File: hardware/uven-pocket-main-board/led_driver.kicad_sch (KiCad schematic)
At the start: 13 parts, among them U12 SIDR392DP-T1-GE3, U13 SIDR392DP-T1-GE3, U4 TPS2HB50BQPWPRQ1

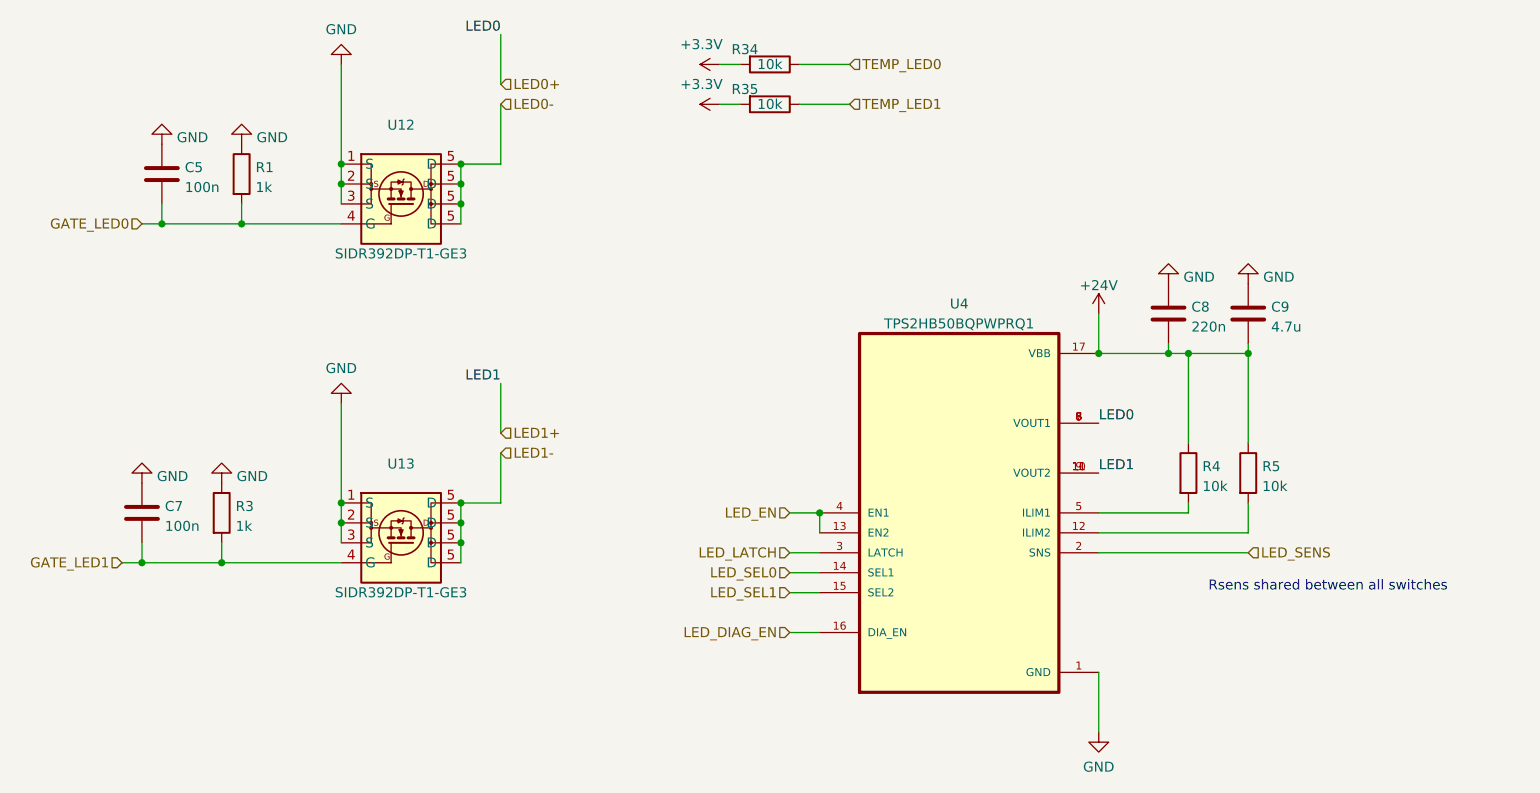
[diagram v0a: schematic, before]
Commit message: uven pocket layout almost finished
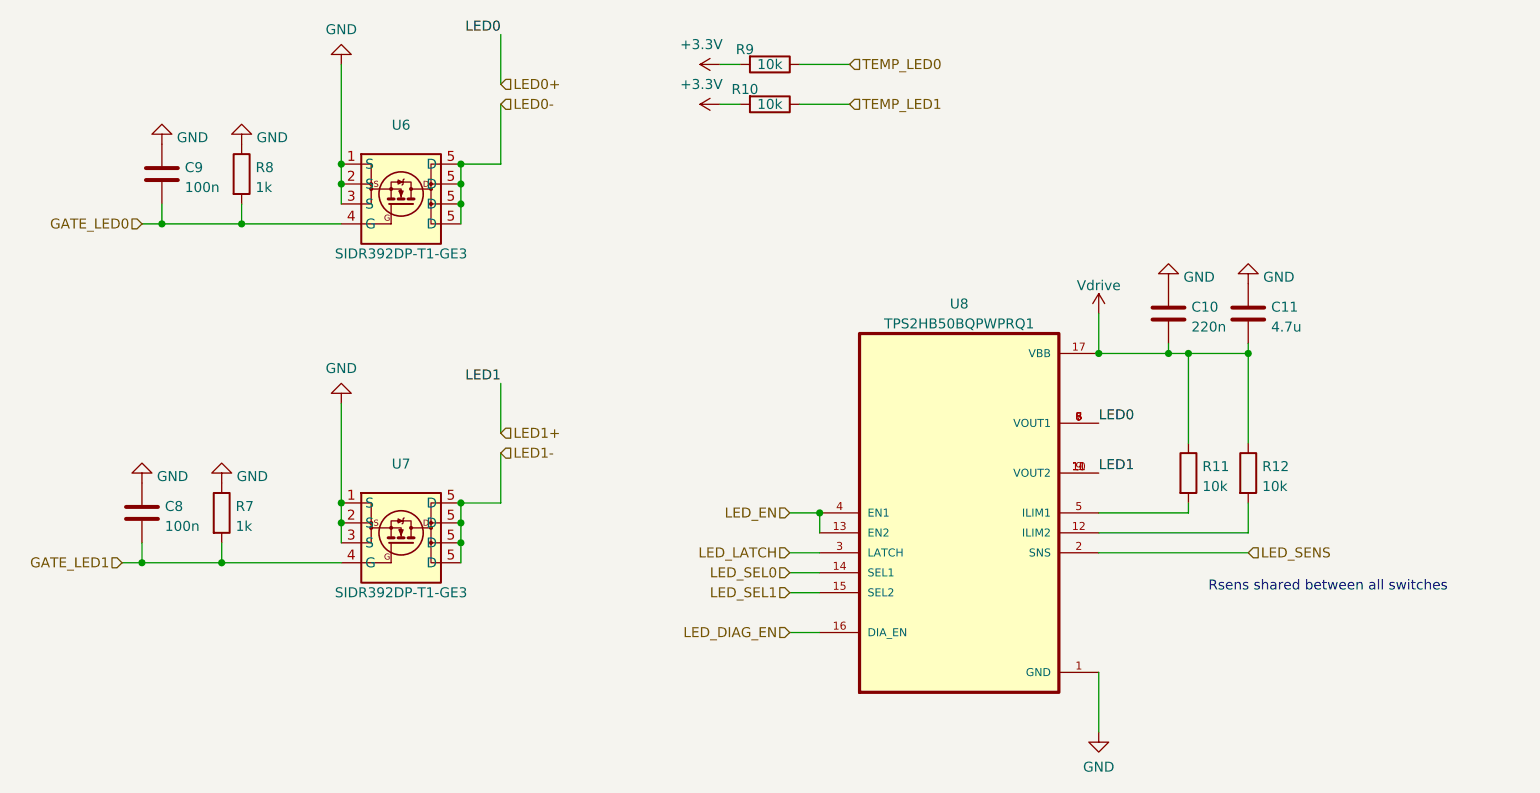
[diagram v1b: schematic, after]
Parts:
- renumbered C8 to C10, C9 to C11, C7 to C8, C5 to C9, R35 to R10, R4 to R11, R5 to R12, R3 to R7, R1 to R8, R34 to R9, U12 to U6, U13 to U7, U4 to U8
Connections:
- net +24V renamed Vdrive
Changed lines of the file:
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@@
   (symbol (lib_id "power:GND") (at 220.98 76.2 180) (unit 1)
     (in_bom yes) (on_board yes) (fields_autoplaced)
-    (property "Reference" "#PWR0119" (id 0) (at 220.98 69.85 0)
+    (property "Reference" "#PWR0136" (id 0) (at 220.98 69.85 0)
       (effects (font (size 1.27 1.27)) hide)
     )
@@
   (symbol (lib_id "uven-mainboard-rescue:R-Device") (at 170.18 48.26 270) (unit 1)
     (in_bom yes) (on_board yes)
-    (property "Reference" "R34" (id 0) (at 167.005 46.355 90))
+    (property "Reference" "R9" (id 0) (at 167.005 46.355 90))
     (property "Value" "10k" (id 1) (at 170.18 48.26 90))
     (property "Footprint" "Resistor_SMD:R_0603_1608Metric_Pad0.98x0.95mm_HandSolder" (id 2) (at 170.18 46.482 90)
@@
   (symbol (lib_id "power:GND") (at 90.17 101.6 180) (unit 1)
     (in_bom yes) (on_board yes) (fields_autoplaced)
-    (property "Reference" "#PWR0122" (id 0) (at 90.17 95.25 0)
+    (property "Reference" "#PWR0139" (id 0) (at 90.17 95.25 0)
       (effects (font (size 1.27 1.27)) hide)
     )
@@
   (symbol (lib_id "power:GND") (at 102.87 58.42 180) (unit 1)
     (in_bom yes) (on_board yes) (fields_autoplaced)
-    (property "Reference" "#PWR0113" (id 0) (at 102.87 52.07 0)
+    (property "Reference" "#PWR0133" (id 0) (at 102.87 52.07 0)
       (effects (font (size 1.27 1.27)) hide)
     )
@@
   (symbol (lib_id "power:+3.3V") (at 163.83 48.26 90) (unit 1)
     (in_bom yes) (on_board yes)
-    (property "Reference" "#PWR0198" (id 0) (at 167.64 48.26 0)
+    (property "Reference" "#PWR0141" (id 0) (at 167.64 48.26 0)
       (effects (font (size 1.27 1.27)) hide)
     )
@@
   (symbol (lib_id "custom:SIDR392DP-T1-GE3") (at 123.19 66.04 0) (unit 1)
     (in_bom yes) (on_board yes)
-    (property "Reference" "U12" (id 0) (at 123.19 55.9902 0))
+    (property "Reference" "U6" (id 0) (at 123.19 55.9902 0))
     (property "Value" "SIDR392DP-T1-GE3" (id 1) (at 123.19 72.39 0))
     (property "Footprint" "custom_lib:PowerPAK SO-8DC" (id 2) (at 123.19 66.04 0)
@@
   (symbol (lib_id "Device:C") (at 92.71 62.23 0) (unit 1)
     (in_bom yes) (on_board yes) (fields_autoplaced)
-    (property "Reference" "C5" (id 0) (at 95.631 61.3953 0)
+    (property "Reference" "C9" (id 0) (at 95.631 61.3953 0)
       (effects (font (size 1.27 1.27)) (justify left))
     )
@@
   (symbol (lib_id "Device:C") (at 231.14 80.01 0) (unit 1)
     (in_bom yes) (on_board yes) (fields_autoplaced)
-    (property "Reference" "C9" (id 0) (at 234.061 79.1753 0)
+    (property "Reference" "C11" (id 0) (at 234.061 79.1753 0)
       (effects (font (size 1.27 1.27)) (justify left))
     )
@@
   (symbol (lib_id "Device:R") (at 223.52 100.33 0) (unit 1)
     (in_bom yes) (on_board yes) (fields_autoplaced)
-    (property "Reference" "R4" (id 0) (at 225.298 99.4953 0)
+    (property "Reference" "R11" (id 0) (at 225.298 99.4953 0)
       (effects (font (size 1.27 1.27)) (justify left))
     )
@@
   (symbol (lib_id "power:GND") (at 115.57 91.44 180) (unit 1)
     (in_bom yes) (on_board yes) (fields_autoplaced)
-    (property "Reference" "#PWR0124" (id 0) (at 115.57 85.09 0)
+    (property "Reference" "#PWR0137" (id 0) (at 115.57 85.09 0)
       (effects (font (size 1.27 1.27)) hide)
     )
@@
   (symbol (lib_id "custom:SIDR392DP-T1-GE3") (at 123.19 109.22 0) (unit 1)
     (in_bom yes) (on_board yes)
-    (property "Reference" "U13" (id 0) (at 123.19 99.1702 0))
+    (property "Reference" "U7" (id 0) (at 123.19 99.1702 0))
     (property "Value" "SIDR392DP-T1-GE3" (id 1) (at 123.19 115.57 0))
     (property "Footprint" "custom_lib:PowerPAK SO-8DC" (id 2) (at 123.19 109.22 0)
@@
   (symbol (lib_id "Device:C") (at 220.98 80.01 0) (unit 1)
     (in_bom yes) (on_board yes) (fields_autoplaced)
-    (property "Reference" "C8" (id 0) (at 223.901 79.1753 0)
+    (property "Reference" "C10" (id 0) (at 223.901 79.1753 0)
       (effects (font (size 1.27 1.27)) (justify left))
     )
@@
     (pin "2")
   )
+  (symbol (lib_id "power:Vdrive") (at 212.09 80.01 0) (unit 1)
+    (in_bom yes) (on_board yes) (fields_autoplaced)
+    (property "Reference" "#PWR0140" (id 0) (at 207.01 83.82 0)
+      (effects (font (size 1.27 1.27)) hide)
+    )
+    (property "Value" "Vdrive" (id 1) (at 212.09 76.4342 0))
+    (property "Footprint" "" (id 2) (at 212.09 80.01 0)
+      (effects (font (size 1.27 1.27)) hide)
+    )
+    (property "Datasheet" "" (id 3) (at 212.09 80.01 0)
+      (effects (font (size 1.27 1.27)) hide)
+    )
+    (pin "1")
+  )
   (symbol (lib_id "Device:C") (at 90.17 105.41 0) (unit 1)
     (in_bom yes) (on_board yes) (fields_autoplaced)
-    (property "Reference" "C7" (id 0) (at 93.091 104.5753 0)
+    (property "Reference" "C8" (id 0) (at 93.091 104.5753 0)
       (effects (font (size 1.27 1.27)) (justify left))
     )
@@
   (symbol (lib_id "power:GND") (at 231.14 76.2 180) (unit 1)
     (in_bom yes) (on_board yes) (fields_autoplaced)
-    (property "Reference" "#PWR0118" (id 0) (at 231.14 69.85 0)
+    (property "Reference" "#PWR0135" (id 0) (at 231.14 69.85 0)
       (effects (font (size 1.27 1.27)) hide)
     )
@@
   (symbol (lib_id "power:GND") (at 100.33 101.6 180) (unit 1)
     (in_bom yes) (on_board yes) (fields_autoplaced)
-    (property "Reference" "#PWR0123" (id 0) (at 100.33 95.25 0)
+    (property "Reference" "#PWR0138" (id 0) (at 100.33 95.25 0)
       (effects (font (size 1.27 1.27)) hide)
     )
@@
   (symbol (lib_id "power:GND") (at 92.71 58.42 180) (unit 1)
     (in_bom yes) (on_board yes) (fields_autoplaced)
-    (property "Reference" "#PWR0112" (id 0) (at 92.71 52.07 0)
+    (property "Reference" "#PWR0132" (id 0) (at 92.71 52.07 0)
       (effects (font (size 1.27 1.27)) hide)
     )
@@
   (symbol (lib_id "power:GND") (at 115.57 48.26 180) (unit 1)
     (in_bom yes) (on_board yes) (fields_autoplaced)
-    (property "Reference" "#PWR0115" (id 0) (at 115.57 41.91 0)
+    (property "Reference" "#PWR0131" (id 0) (at 115.57 41.91 0)
       (effects (font (size 1.27 1.27)) hide)
     )
@@
   (symbol (lib_id "uven-mainboard-rescue:R-Device") (at 170.18 53.34 270) (unit 1)
     (in_bom yes) (on_board yes)
-    (property "Reference" "R35" (id 0) (at 167.005 51.435 90))
+    (property "Reference" "R10" (id 0) (at 167.005 51.435 90))
     (property "Value" "10k" (id 1) (at 170.18 53.34 90))
     (property "Footprint" "Resistor_SMD:R_0603_1608Metric_Pad0.98x0.95mm_HandSolder" (id 2) (at 170.18 51.562 90)
@@
   (symbol (lib_id "Device:R") (at 100.33 105.41 0) (unit 1)
     (in_bom yes) (on_board yes) (fields_autoplaced)
-    (property "Reference" "R3" (id 0) (at 102.108 104.5753 0)
+    (property "Reference" "R7" (id 0) (at 102.108 104.5753 0)
       (effects (font (size 1.27 1.27)) (justify left))
     )
@@
   (symbol (lib_id "TPS2HB50BQPWPRQ1:TPS2HB50BQPWPRQ1") (at 194.31 105.41 0) (unit 1)
     (in_bom yes) (on_board yes) (fields_autoplaced)
-    (property "Reference" "U4" (id 0) (at 194.31 78.7722 0))
+    (property "Reference" "U8" (id 0) (at 194.31 78.7722 0))
     (property "Value" "TPS2HB50BQPWPRQ1" (id 1) (at 194.31 81.3091 0))
     (property "Footprint" "custom_lib:SOP65P640X120-17N" (id 2) (at 194.31 105.41 0)
@@
   (symbol (lib_id "power:+3.3V") (at 163.83 53.34 90) (unit 1)
     (in_bom yes) (on_board yes)
-    (property "Reference" "#PWR0199" (id 0) (at 167.64 53.34 0)
+    (property "Reference" "#PWR0142" (id 0) (at 167.64 53.34 0)
       (effects (font (size 1.27 1.27)) hide)
     )
@@
   (symbol (lib_id "Device:R") (at 102.87 62.23 0) (unit 1)
     (in_bom yes) (on_board yes) (fields_autoplaced)
-    (property "Reference" "R1" (id 0) (at 104.648 61.3953 0)
+    (property "Reference" "R8" (id 0) (at 104.648 61.3953 0)
       (effects (font (size 1.27 1.27)) (justify left))
     )
@@
   (symbol (lib_id "Device:R") (at 231.14 100.33 0) (unit 1)
     (in_bom yes) (on_board yes) (fields_autoplaced)
-    (property "Reference" "R5" (id 0) (at 232.918 99.4953 0)
+    (property "Reference" "R12" (id 0) (at 232.918 99.4953 0)
       (effects (font (size 1.27 1.27)) (justify left))
     )
@@
     (pin "2")
   )
-  (symbol (lib_id "power:+24V") (at 212.09 80.01 0) (unit 1)
-    (in_bom yes) (on_board yes) (fields_autoplaced)
-    (property "Reference" "#PWR0120" (id 0) (at 212.09 83.82 0)
-      (effects (font (size 1.27 1.27)) hide)
-    )
-    (property "Value" "+24V" (id 1) (at 212.09 76.4342 0))
-    (property "Footprint" "" (id 2) (at 212.09 80.01 0)
-      (effects (font (size 1.27 1.27)) hide)
-    )
-    (property "Datasheet" "" (id 3) (at 212.09 80.01 0)
-      (effects (font (size 1.27 1.27)) hide)
-    )
-    (pin "1")
-  )
   (symbol (lib_id "power:GND") (at 212.09 133.35 0) (unit 1)
     (in_bom yes) (on_board yes) (fields_autoplaced)
-    (property "Reference" "#PWR0121" (id 0) (at 212.09 139.7 0)
-      (effects (font (size 1.27 1.27)) hide)
-    )
+    (property "Reference" "#PWR0134" (id 0) (at 212.09 139.7 0)
+      (effects (font (size 1.27 1.27)) hide)
+    )
